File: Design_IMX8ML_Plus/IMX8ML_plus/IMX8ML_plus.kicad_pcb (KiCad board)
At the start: 6 copper layers, 50 x 82 mm, 154 parts, among them J1 DF40C-100DP-0.4V_51_, J2 DF40C-100DP-0.4V_51_, J3 DF40C-100DP-0.4V_51_, U1 MIMX8ML8CVNKZAB, U2 MT53E1536M32D4DT-046 WT:A, U3 SDINBDG4-8G, U4 PCA9450CHNY, U5 MT25QUxxxxxx1xW7, Y1 32.768KHz, Y2 24MHz, Y3 32.768KHz

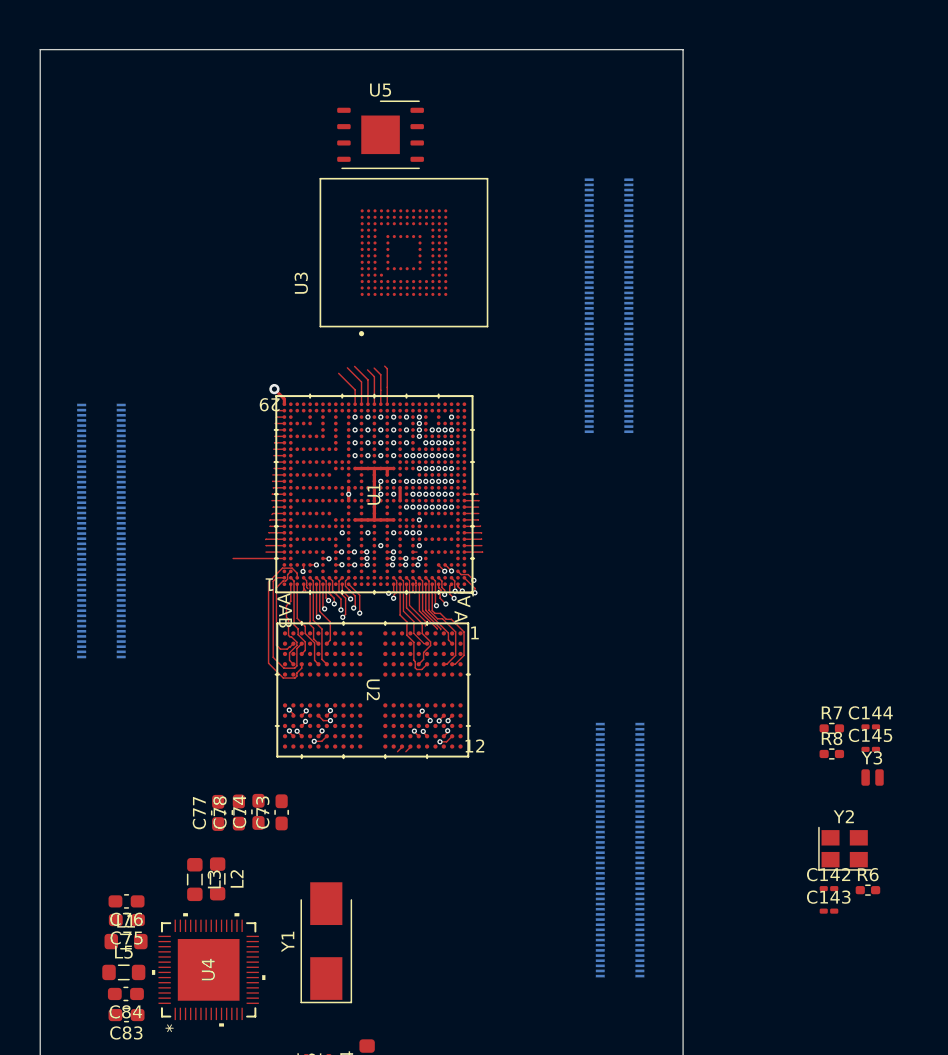
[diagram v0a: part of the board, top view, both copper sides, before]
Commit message: Update schematic and add ethernet interface ksz9131rn
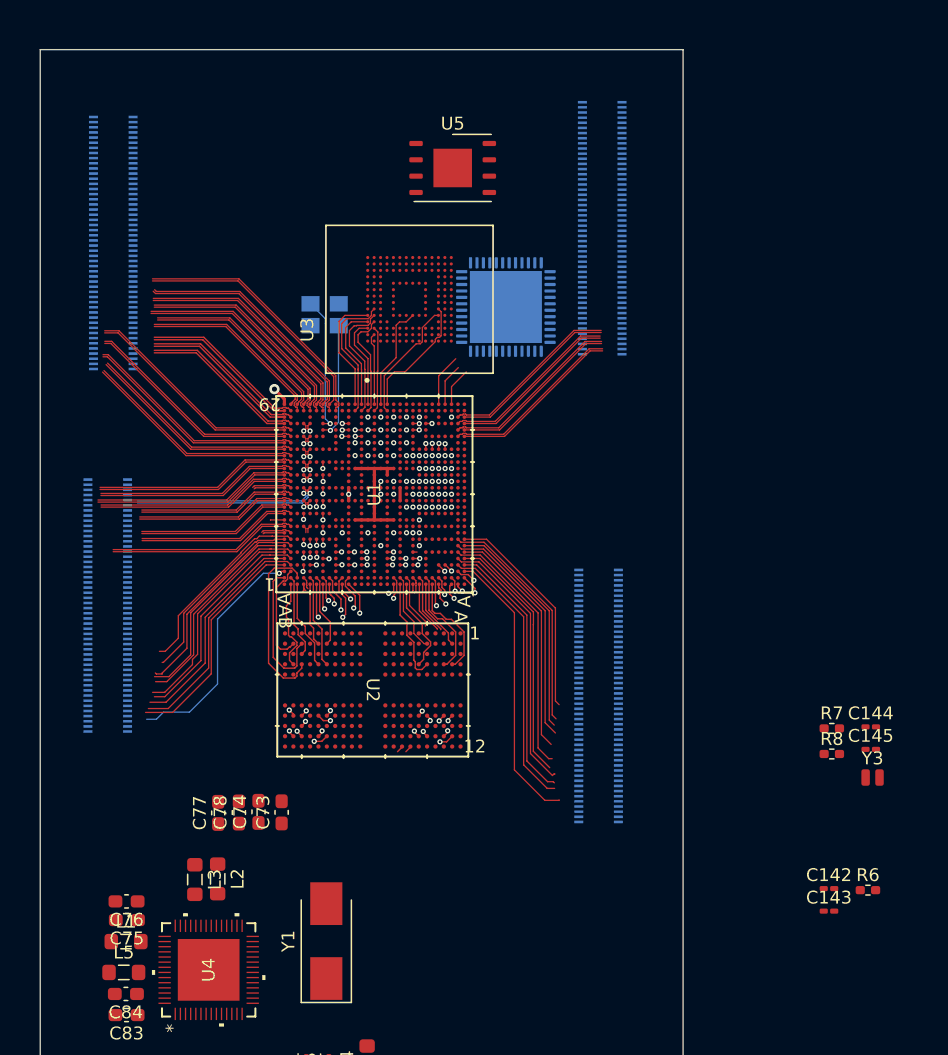
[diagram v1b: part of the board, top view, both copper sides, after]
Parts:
- added J4: DF40C-100DP-0.4V_51_, _W_SBC:HIROSE_DF40C-100DS-0.4V_51_, B.Cu at (153.4, 105.3)
- added U6: KSZ9131RNXI, Package_DFN_QFN:QFN-48-1EP_7x7mm_P0.5mm_EP5.6x5.6mm, B.Cu at (146.2, 75.0)
- Y2: moved to B.Cu
- moved Y2 58.0 mm to (132.1, 75.6), turned to 180 degrees
- moved J1 44.2 mm to (115.2, 98.2)
- moved J2 22.4 mm to (115.7, 70.0), turned to 90 degrees
- moved U5 6.17 mm to (142.1, 64.2)
- moved J3 6.05 mm to (153.7, 68.9), turned to 90 degrees
- moved U3 3.66 mm to (138.7, 74.4)
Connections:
- J1 pad 17: GPIO1_IO00 -> unconnected-(J1-Pad17)
- J1 pad 19: GPIO1_IO01 -> unconnected-(J1-Pad19)
- J1 pad 21: GPIO1_IO02 -> unconnected-(J1-Pad21)
- J1 pad 22: USB1_D_N -> unconnected-(J1-Pad22)
- J1 pad 23: GPIO1_IO03 -> unconnected-(J1-Pad23)
- J1 pad 24: USB1_D_P -> unconnected-(J1-Pad24)
- J1 pad 25: GPIO1_IO04 -> unconnected-(J1-Pad25)
- J1 pad 27: GPIO1_IO05 -> unconnected-(J1-Pad27)
- J1 pad 28: USB1_RX_N -> unconnected-(J1-Pad28)
- J1 pad 29: GPIO1_IO06 -> unconnected-(J1-Pad29)
- J1 pad 30: USB1_RX_P -> unconnected-(J1-Pad30)
- J1 pad 31: GPIO1_IO07 -> unconnected-(J1-Pad31)
- J1 pad 32: USB1_TX_N -> unconnected-(J1-Pad32)
- J1 pad 33: GPIO1_IO08 -> unconnected-(J1-Pad33)
- J1 pad 34: USB1_TX_P -> unconnected-(J1-Pad34)
- J1 pad 35: GPIO1_IO09 -> unconnected-(J1-Pad35)
- J1 pad 37: GPIO1_IO10 -> unconnected-(J1-Pad37)
- J1 pad 38: USB1_BUS -> unconnected-(J1-Pad38)
- J1 pad 39: GPIO1_IO11 -> PCIE_TXN_P
- J1 pad 41: GPIO1_IO12 -> PCIE_TXN_N
- J1 pad 42: PCIE_REF_PAD_CLK_N -> unconnected-(J1-Pad42)
- J1 pad 43: GPIO1_IO13 -> PCIE_RXN_P
- J1 pad 44: PCIE_REF_PAD_CLK_P -> unconnected-(J1-Pad44)
- J1 pad 45: GPIO1_IO14 -> PCIE_RXN_N
- J1 pad 47: GPIO1_IO15 -> unconnected-(J1-Pad47)
- J1 pad 48: PCIE_RXN_N -> unconnected-(J1-Pad48)
- J1 pad 49: unconnected-(J1-Pad49) -> PCIE_REF_PAD_CLK_P
- J1 pad 50: PCIE_RXN_P -> unconnected-(J1-Pad50)
- J1 pad 51: USB2_D_N -> PCIE_REF_PAD_CLK_N
- J1 pad 52: PCIE_TXN_N -> unconnected-(J1-Pad52)
- J1 pad 53: USB2_D_P -> unconnected-(J1-Pad53)
- J1 pad 54: PCIE_TXN_P -> unconnected-(J1-Pad54)
- J1 pad 57: USB2_RX_N -> unconnected-(J1-Pad57)
- J1 pad 58: CSI2_D0_N -> unconnected-(J1-Pad58)
- J1 pad 59: USB2_RX_P -> unconnected-(J1-Pad59)
- J1 pad 60: CSI2_D0_P -> unconnected-(J1-Pad60)
- J1 pad 61: USB2_TX_N -> GPIO1_IO00
- J1 pad 62: CSI2_D1_N -> unconnected-(J1-Pad62)
- J1 pad 63: USB2_TX_P -> GPIO1_IO01
- J1 pad 64: CSI2_D1_P -> unconnected-(J1-Pad64)
- J1 pad 65: unconnected-(J1-Pad65) -> GPIO1_IO02
- J1 pad 66: CSI2_D2_N -> unconnected-(J1-Pad66)
- J1 pad 67: USB2_BUS -> unconnected-(J1-Pad67)
- J1 pad 68: CSI2_D2_P -> unconnected-(J1-Pad68)
- J1 pad 70: CSI2_D3_N -> unconnected-(J1-Pad70)
- J1 pad 71: DSI1_D0_N -> GPIO1_IO05
- J1 pad 72: DSI2_D3_P -> unconnected-(J1-Pad72)
- J1 pad 73: DSI1_D0_P -> GPIO1_IO06
- J1 pad 75: DSI1_D1_N -> GPIO1_IO07
- J1 pad 76: CSI1_D0_N -> unconnected-(J1-Pad76)
- J1 pad 77: DSI1_D1_P -> GPIO1_IO08
- J1 pad 78: CSI1_D0_P -> unconnected-(J1-Pad78)
- J1 pad 79: DSI1_D2_N -> GPIO1_IO09
- J1 pad 80: CSI1_D1_N -> unconnected-(J1-Pad80)
- J1 pad 81: DSI1_D2_P -> GPIO1_IO10
- J1 pad 82: CSI1_D1_P -> unconnected-(J1-Pad82)
- J1 pad 83: DSI1_D3_N -> GPIO1_IO11
- J1 pad 84: CSI1_D2_N -> unconnected-(J1-Pad84)
- J1 pad 85: DSI1_D3_P -> GPIO1_IO12
- J1 pad 86: CSI1_D2_P -> unconnected-(J1-Pad86)
- J1 pad 87: unconnected-(J1-Pad87) -> GPIO1_IO13
- J1 pad 88: CSI1_D3_N -> unconnected-(J1-Pad88)
- J1 pad 89: unconnected-(J1-Pad89) -> GPIO1_IO14
- J1 pad 90: CSI1_D3_P -> unconnected-(J1-Pad90)
- J1 pad 91: unconnected-(J1-Pad91) -> GPIO1_IO15
- J2 pad 10: SAI5_RXD2 -> JTAG_TMS
- J2 pad 100: ENET_TD3 -> unconnected-(J2-Pad100)
- J2 pad 11: SAI1_TXD0 -> HDM_TX2_N
- J2 pad 12: SAI5_RXD3 -> JTAG_TDO
- J2 pad 13: SAI1_TXD1 -> HDM_TX1_P
- J2 pad 14: SAI5_MCLK -> JTAG_TDI
- J2 pad 15: SAI1_TXD2 -> HDM_TX1_N
- J2 pad 16: SAI5_RXC -> JTAG_TCK
- J2 pad 17: SAI1_TXD3 -> HDM_TX0_P
- J2 pad 18: SAI5_RXFS -> JTAG_MOD
- J2 pad 19: SAI1_TXD4 -> HDM_TX0_N
- J2 pad 21: SAI1_TXD5 -> unconnected-(J2-Pad21)
- J2 pad 22: unconnected-(J2-Pad22) -> CLKOUT2
- J2 pad 23: SAI1_TXD6 -> HDM_HPD
- J2 pad 24: SAI2_MCLK -> CLKOUT1
- J2 pad 25: SAI1_RXD7 -> HDM_DDC_SDA
- J2 pad 26: SAI2_RXC -> CLKIN2
- J2 pad 27: unconnected-(J2-Pad27) -> HDM_DDC_SCL
- J2 pad 28: SAI2_RXFS -> CLKIN1
- J2 pad 29: SAI1_MCLK -> HDM_CEC
- J2 pad 30: SAI2_TXC -> unconnected-(J2-Pad30)
- J2 pad 31: SAI1_RXC -> unconnected-(J2-Pad31)
- J2 pad 32: SAI2_TXFS -> BOOT_MODE3
- J2 pad 33: SAI1_RXFS -> unconnected-(J2-Pad33)
- J2 pad 34: unconnected-(J2-Pad34) -> BOOT_MODE2
- J2 pad 35: SAI1_TXC -> unconnected-(J2-Pad35)
- J2 pad 36: SAI2_RXD0 -> BOOT_MODE1
- J2 pad 37: SAi1_TXFS -> LVDS1_CLK_N
- J2 pad 38: SAI2_TXD0 -> BOOT_MODE0
- J2 pad 39: I2C1_SCL -> LVDS1_CLK_P
- J2 pad 41: I2C1_SDA -> LVDS1_D3_P
- J2 pad 42: SAI3_MCLK -> unconnected-(J2-Pad42)
- J2 pad 43: unconnected-(J2-Pad43) -> LVDS1_D3_N
- J2 pad 44: SAI3_RXC -> SDC1_STROBE
- J2 pad 45: I2C3_SDA -> LVDS1_D2_P
- J2 pad 46: SAI3_RXD -> SDC1_RESET_B
- J2 pad 47: I2C3_SCL -> LVDS1_D2_N
- J2 pad 48: SAI3_RXFS -> SDC1_DATA7
- J2 pad 49: unconnected-(J2-Pad49) -> LVDS1_D1_P
- J2 pad 5: SAI1_RXD5 -> HDM_TXC_P
- J2 pad 50: SAI3_TXC -> SDC1_DATA6
- J2 pad 51: I2C2_SCL -> LVDS1_D1_N
- J2 pad 52: SAI3_TXD -> SDC1_DATA5
- J2 pad 53: I2C2_SDA -> LVDS1_D0_P
- J2 pad 54: SAI3_TXFS -> SDC1_DATA4
- J2 pad 55: unconnected-(J2-Pad55) -> LVDS1_D0_N
- J2 pad 56: unconnected-(J2-Pad56) -> SDC1_DATA3
- J2 pad 57: I2C4_SDA -> unconnected-(J2-Pad57)
- J2 pad 58: unconnected-(J2-Pad58) -> SDC1_DATA2
- J2 pad 59: I2C4_SCL -> LVDS0_CLK_P
- J2 pad 6: SAI5_RXD0 -> unconnected-(J2-Pad6)
- J2 pad 60: unconnected-(J2-Pad60) -> SDC1_DATA1
- J2 pad 61: unconnected-(J2-Pad61) -> LVDS0_CLK_N
- J2 pad 62: SAI1_RXD0 -> SDC1_DATA0
- J2 pad 63: UART1_RXD -> LVDS0_D3_P
- J2 pad 64: SAI1_RXD1 -> SDC1_CMD
- J2 pad 65: UART1_TXD -> LVDS0_D3_N
- J2 pad 66: SAI1_RXD2 -> SDC1_CLK
- J2 pad 67: UART2_RXD -> LVDS0_D2_P
- J2 pad 68: SAI1_RXD3 -> unconnected-(J2-Pad68)
- J2 pad 69: UART2_TXD -> LVDS0_D2_N
- J2 pad 7: SAI1_RXD6 -> HDM_TXC_N
- J2 pad 70: SAI1_RXD4 -> SDC2_WP
- J2 pad 71: UART3_RXD -> LVDS0_D1_P
- J2 pad 72: unconnected-(J2-Pad72) -> SDC2_RESET_B
- J2 pad 73: UART3_TXD -> LVDS0_D1_N
- J2 pad 74: ENET_TXC -> SDC2_DATA3
- J2 pad 75: UART4_RXD -> LVDS0_D0_P
- J2 pad 76: ENET_TX_CTL -> SDC2_DATA2
- J2 pad 77: UART4_TXD -> LVDS0_D0_N
- J2 pad 78: ENET_RXC -> SDC2_DATA1
- J2 pad 8: SAI5_RXD1 -> unconnected-(J2-Pad8)
- J2 pad 80: ENET_RX_CTL -> SDC2_DATA0
- J2 pad 82: ENET_MDIO -> SDC2_CMD
- J2 pad 83: CSI1_CLK_P -> unconnected-(J2-Pad83)
- J2 pad 84: ENET_MDC -> SDC2_CLK
- J2 pad 85: CSI1_CLK_N -> unconnected-(J2-Pad85)
- J2 pad 86: ENET_RD0 -> SDC2_CD_B
- J2 pad 88: ENET_RD1 -> unconnected-(J2-Pad88)
- J2 pad 89: CSI2_CLK_P -> unconnected-(J2-Pad89)
- J2 pad 9: SAI1_RXD7 -> HDM_TX2_P
- J2 pad 90: ENET_RD2 -> unconnected-(J2-Pad90)
- J2 pad 91: CSI2_CLK_N -> unconnected-(J2-Pad91)
- J2 pad 92: ENET_RD3 -> unconnected-(J2-Pad92)
- J2 pad 94: ENET_TD0 -> unconnected-(J2-Pad94)
- J2 pad 95: DSI1_CLK_P -> unconnected-(J2-Pad95)
- J2 pad 96: ENET_TD1 -> unconnected-(J2-Pad96)
- J2 pad 97: DSI1_CLK_N -> unconnected-(J2-Pad97)
- J2 pad 98: ENET_TD2 -> unconnected-(J2-Pad98)
- J3 pad 11: LVDS0_D0_N -> unconnected-(J3-Pad11)
- J3 pad 13: LVDS0_D0_P -> unconnected-(J3-Pad13)
- J3 pad 15: LVDS0_D1_N -> unconnected-(J3-Pad15)
- J3 pad 16: SDC2_CD_B -> unconnected-(J3-Pad16)
- J3 pad 17: LVDS0_D1_P -> unconnected-(J3-Pad17)
- J3 pad 18: SDC2_CLK -> unconnected-(J3-Pad18)
- J3 pad 19: LVDS0_D2_N -> unconnected-(J3-Pad19)
- J3 pad 20: SDC2_CMD -> unconnected-(J3-Pad20)
- J3 pad 21: LVDS0_D2_P -> unconnected-(J3-Pad21)
- J3 pad 22: SDC2_DATA0 -> unconnected-(J3-Pad22)
- J3 pad 23: LVDS0_D3_N -> unconnected-(J3-Pad23)
- J3 pad 24: SDC2_DATA1 -> unconnected-(J3-Pad24)
- J3 pad 25: LVDS0_D3_P -> unconnected-(J3-Pad25)
- J3 pad 26: SDC2_DATA2 -> unconnected-(J3-Pad26)
- J3 pad 27: LVDS0_CLK_N -> unconnected-(J3-Pad27)
- J3 pad 28: SDC2_DATA3 -> unconnected-(J3-Pad28)
- J3 pad 29: LVDS0_CLK_P -> SAI1_RXD5
- J3 pad 30: SDC2_RESET_B -> unconnected-(J3-Pad30)
- J3 pad 31: unconnected-(J3-Pad31) -> SAI1_RXD6
- J3 pad 32: SDC2_WP -> SAI5_RXD0
- J3 pad 33: LVDS1_D0_N -> SAI1_RXD7
- J3 pad 34: unconnected-(J3-Pad34) -> SAI5_RXD1
- J3 pad 35: LVDS1_D0_P -> SAI1_TXD0
- J3 pad 36: SDC1_CLK -> SAI5_RXD2
- J3 pad 37: LVDS1_D1_N -> SAI1_TXD1
- J3 pad 38: SDC1_CMD -> SAI5_RXD3
- J3 pad 39: LVDS1_D1_P -> SAI1_TXD2
- J3 pad 40: SDC1_DATA0 -> SAI5_MCLK
- J3 pad 41: LVDS1_D2_N -> SAI1_TXD3
- J3 pad 42: SDC1_DATA1 -> SAI5_RXC
- J3 pad 43: LVDS1_D2_P -> SAI1_TXD4
- J3 pad 44: SDC1_DATA2 -> SAI5_RXFS
- J3 pad 45: LVDS1_D3_N -> SAI1_TXD5
- J3 pad 46: SDC1_DATA3 -> unconnected-(J3-Pad46)
- J3 pad 47: LVDS1_D3_P -> SAI1_TXD6
- J3 pad 48: SDC1_DATA4 -> unconnected-(J3-Pad48)
- J3 pad 49: LVDS1_CLK_P -> SAI1_RXD7
- J3 pad 50: SDC1_DATA5 -> unconnected-(J3-Pad50)
- J3 pad 51: LVDS1_CLK_N -> unconnected-(J3-Pad51)
- J3 pad 52: SDC1_DATA6 -> unconnected-(J3-Pad52)
- J3 pad 54: SDC1_DATA7 -> unconnected-(J3-Pad54)
- J3 pad 56: SDC1_RESET_B -> unconnected-(J3-Pad56)
- J3 pad 58: SDC1_STROBE -> unconnected-(J3-Pad58)
- J3 pad 59: HDM_CEC -> unconnected-(J3-Pad59)
- J3 pad 61: HDM_DDC_SCL -> unconnected-(J3-Pad61)
- J3 pad 63: HDM_DDC_SDA -> unconnected-(J3-Pad63)
- J3 pad 64: BOOT_MODE0 -> unconnected-(J3-Pad64)
- J3 pad 65: HDM_HPD -> unconnected-(J3-Pad65)
- J3 pad 66: BOOT_MODE1 -> TXRXA_N
- J3 pad 68: BOOT_MODE2 -> TXRXA_P
- J3 pad 69: HDM_TX0_N -> unconnected-(J3-Pad69)
- J3 pad 70: BOOT_MODE3 -> unconnected-(J3-Pad70)
- J3 pad 71: HDM_TX0_P -> unconnected-(J3-Pad71)
- J3 pad 72: unconnected-(J3-Pad72) -> TXRXB_N
- J3 pad 73: HDM_TX1_N -> unconnected-(J3-Pad73)
- J3 pad 74: CLKIN1 -> TXRXB_P
- J3 pad 75: HDM_TX1_P -> unconnected-(J3-Pad75)
- J3 pad 76: CLKIN2 -> unconnected-(J3-Pad76)
- J3 pad 77: HDM_TX2_N -> unconnected-(J3-Pad77)
- J3 pad 78: CLKOUT1 -> TXRXC_P
- J3 pad 79: HDM_TX2_P -> unconnected-(J3-Pad79)
- J3 pad 80: CLKOUT2 -> TXRXC_N
- J3 pad 81: HDM_TXC_N -> unconnected-(J3-Pad81)
- J3 pad 83: HDM_TXC_P -> unconnected-(J3-Pad83)
- J3 pad 84: JTAG_MOD -> TXRXD_N
- J3 pad 86: JTAG_TCK -> TXRXD_P
- J3 pad 88: JTAG_TDI -> unconnected-(J3-Pad88)
- J3 pad 90: JTAG_TDO -> unconnected-(J3-Pad90)
- J3 pad 92: JTAG_TMS -> unconnected-(J3-Pad92)
- U1 pad A11: USB1_BUS -> USB1_VBUS
- U1 pad A21: DSI2_D3_P -> CSI2_D3_P
- U1 pad AC22: HDM_DDC_SCL -> HDMI_DDC_SCL
- U1 pad AD22: HDM_CEC -> HDMI_CEC
- U1 pad AE22: HDM_HPD -> HDMI_HPD
- U1 pad AF22: HDM_DDC_SDA -> HDMI_DDC_SDA
- U1 pad AH24: HDM_TXC_P -> HDMI_TXC_P
- U1 pad AH25: HDM_TX0_P -> HDMI_TX0_P
- U1 pad AH26: HDM_TX1_P -> HDMI_TX1_P
- U1 pad AH27: HDM_TX2_P -> HDMI_TX2_P
- U1 pad AJ24: HDM_TXC_N -> HDMI_TXC_N
- U1 pad AJ25: HDM_TX0_N -> HDMI_TX0_N
- U1 pad AJ26: HDM_TX1_N -> HDMI_TX1_N
- U1 pad AJ27: HDM_TX2_N -> HDMI_TX2_N
- U1 pad D12: USB2_BUS -> USB2_VBUS
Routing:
- net /Processor/storage/QSPIA_DATA3: track 0.00 -> 33.5 mm, vias 0 -> 1
- net /Processor/storage/QSPIA_SCLK: track 0.00 -> 30.4 mm, vias 0 -> 1
- net /Processor/storage/QSPIA_DATA0: track 0.00 -> 29.7 mm, vias 0 -> 1
- net /Processor/storage/QSPIA_nSS0: track 0.00 -> 26.0 mm, vias 0 -> 1
- net /Processor/storage/QSPIA_DATA1: track 0.00 -> 25.3 mm, vias 0 -> 1
- net /Processor/storage/QSPIA_DATA2: track 0.00 -> 24.4 mm, vias 0 -> 1
- net CSI1_D0_N: track 0.00 -> 23.7 mm, vias 0 -> 1
- net CSI1_D0_P: track 0.00 -> 23.3 mm, vias 0 -> 1
- net CSI1_D1_N: track 0.00 -> 22.7 mm, vias 0 -> 1
- net CSI1_D1_P: track 0.00 -> 22.3 mm, vias 0 -> 1
- net UART1_TXD: track 0.00 -> 21.9 mm
- net UART2_TXD: track 0.00 -> 21.5 mm
- net GPIO1_IO07: track 0.00 -> 21.2 mm, vias 0 -> 1
- net CSI1_CLK_N: track 0.00 -> 21.0 mm, vias 0 -> 1
- net UART4_TXD: track 0.00 -> 21.0 mm
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
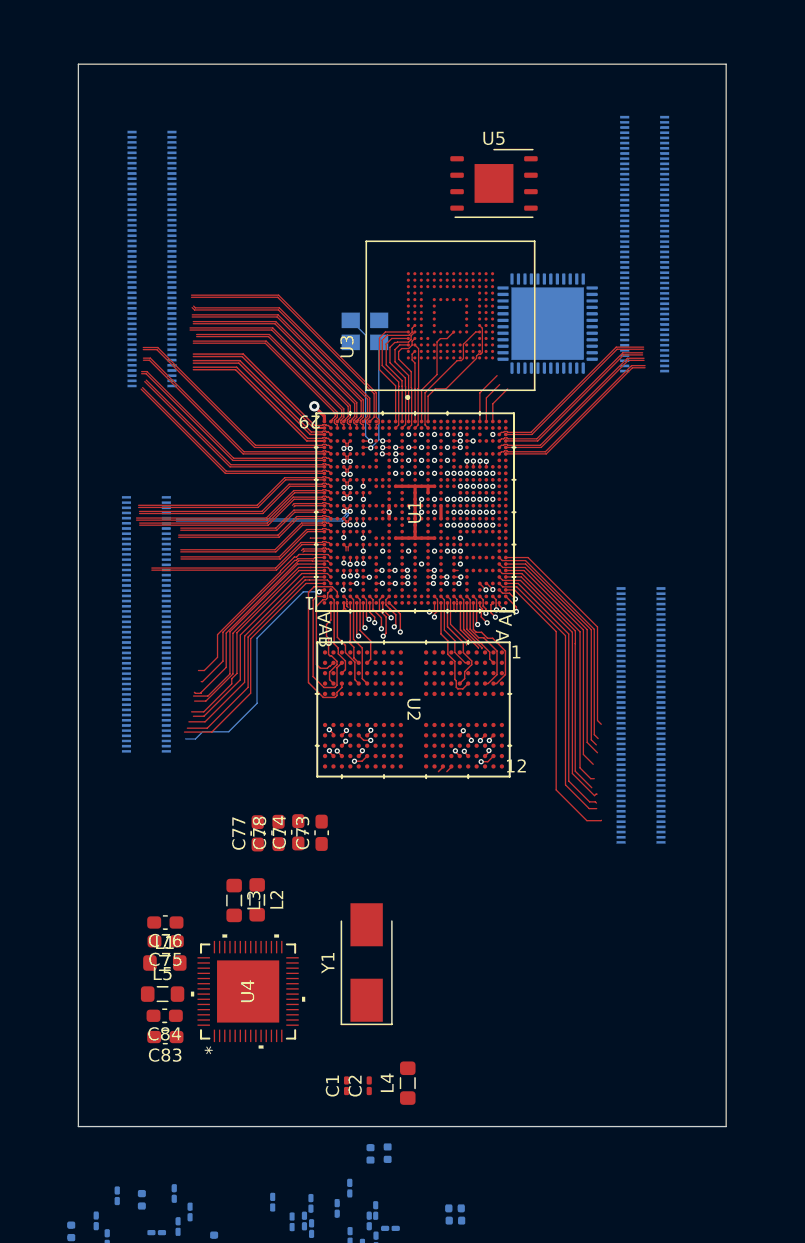
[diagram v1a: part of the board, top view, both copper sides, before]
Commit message: Add power layer
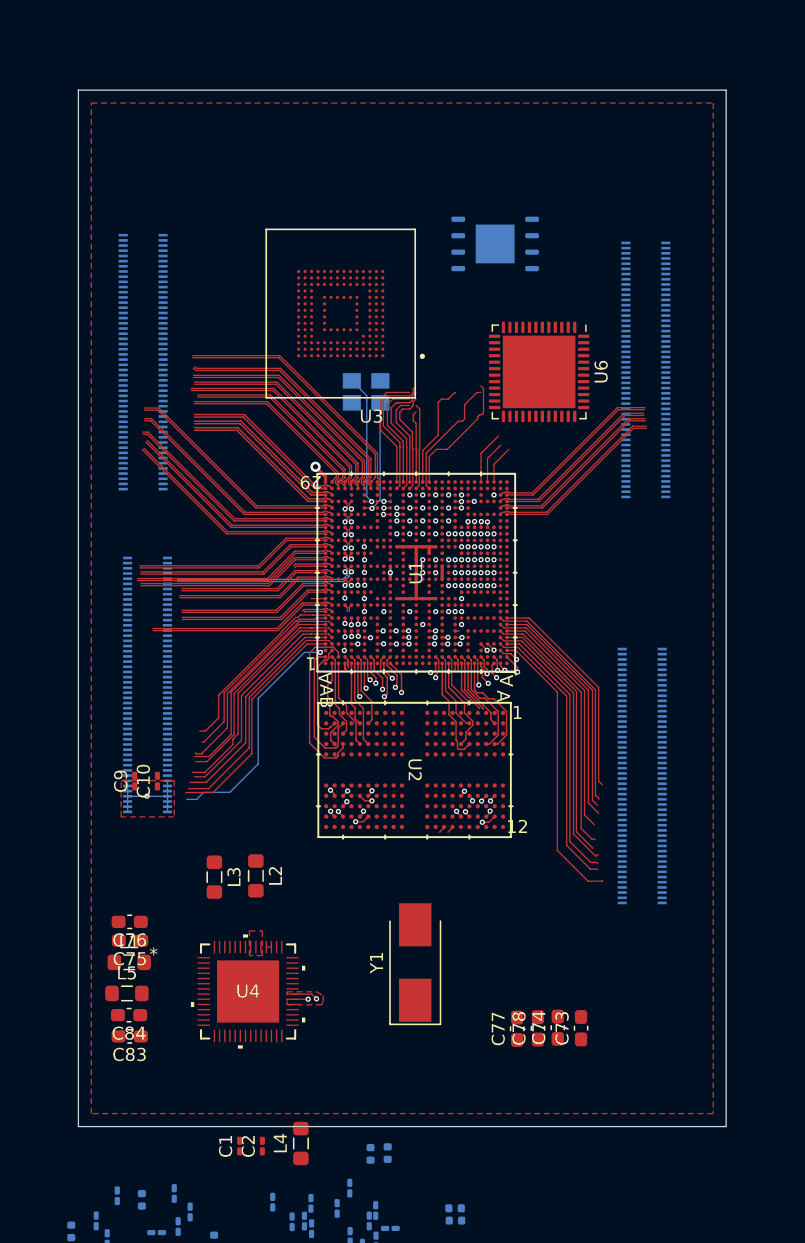
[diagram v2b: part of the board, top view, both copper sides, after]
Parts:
- added C10: 10uF, Capacitor_SMD:C_0201_0603Metric_Pad0.64x0.40mm_HandSolder, F.Cu at (116.1, 110.3)
- added C9: 10uF, Capacitor_SMD:C_0201_0603Metric_Pad0.64x0.40mm_HandSolder, F.Cu at (114.3, 110.3)
- U5: moved to B.Cu
- U6: moved to F.Cu
- moved C74 25.1 mm to (147.0, 129.4)
- moved C73 25.1 mm to (148.8, 129.4)
- moved C77 25.1 mm to (143.9, 129.4)
- moved C78 25.1 mm to (145.5, 129.4)
- moved J3 9.71 mm to (153.8, 78.6)
- moved L4 9.47 mm to (127.2, 138.3)
- moved C1 9.47 mm to (122.5, 138.5)
- moved C2 9.47 mm to (124.2, 138.5)
- moved U3 8.47 mm to (130.2, 74.2), turned to 180 degrees
- moved J2 7.99 mm to (115.0, 78.0)
- moved J1 4.67 mm to (115.3, 102.9)
- moved J4 4.67 mm to (153.5, 109.9)
- moved U1 4.67 mm to (136.1, 94.2)
- moved Y2 4.67 mm to (132.2, 80.3)
- moved U5 4.67 mm to (142.2, 68.9), turned to 180 degrees
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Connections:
- J1 pad 100: unconnected-(J1-Pad100) -> VDD_SYS
- J1 pad 11: unconnected-(J1-Pad11) -> PCIE_TXN_P
- J1 pad 13: unconnected-(J1-Pad13) -> PCIE_TXN_N
- J1 pad 15: unconnected-(J1-Pad15) -> PCIE_RXN_P
- J1 pad 17: unconnected-(J1-Pad17) -> PCIE_RXN_N
- J1 pad 21: unconnected-(J1-Pad21) -> PCIE_REF_PAD_CLK_P
- J1 pad 23: unconnected-(J1-Pad23) -> PCIE_REF_PAD_CLK_N
- J1 pad 33: unconnected-(J1-Pad33) -> GPIO1_IO00
- J1 pad 35: unconnected-(J1-Pad35) -> GPIO1_IO01
- J1 pad 37: unconnected-(J1-Pad37) -> GPIO1_IO02
- J1 pad 39: PCIE_TXN_P -> unconnected-(J1-Pad39)
- J1 pad 41: PCIE_TXN_N -> unconnected-(J1-Pad41)
- J1 pad 43: PCIE_RXN_P -> GPIO1_IO05
- J1 pad 45: PCIE_RXN_N -> GPIO1_IO06
- J1 pad 47: unconnected-(J1-Pad47) -> GPIO1_IO07
- J1 pad 49: PCIE_REF_PAD_CLK_P -> GPIO1_IO08
- J1 pad 51: PCIE_REF_PAD_CLK_N -> GPIO1_IO09
- J1 pad 53: unconnected-(J1-Pad53) -> GPIO1_IO10
- J1 pad 55: unconnected-(J1-Pad55) -> GPIO1_IO11
- J1 pad 57: unconnected-(J1-Pad57) -> GPIO1_IO12
- J1 pad 59: unconnected-(J1-Pad59) -> GPIO1_IO13
- J1 pad 61: GPIO1_IO00 -> GPIO1_IO14
- J1 pad 63: GPIO1_IO01 -> GPIO1_IO15
- J1 pad 65: GPIO1_IO02 -> unconnected-(J1-Pad65)
- J1 pad 71: GPIO1_IO05 -> unconnected-(J1-Pad71)
- J1 pad 73: GPIO1_IO06 -> unconnected-(J1-Pad73)
- J1 pad 75: GPIO1_IO07 -> GND
- J1 pad 76: unconnected-(J1-Pad76) -> GND
- J1 pad 77: GPIO1_IO08 -> GND
- J1 pad 78: unconnected-(J1-Pad78) -> GND
- J1 pad 79: GPIO1_IO09 -> GND
- J1 pad 80: unconnected-(J1-Pad80) -> GND
- J1 pad 81: GPIO1_IO10 -> GND
- J1 pad 82: unconnected-(J1-Pad82) -> GND
- J1 pad 83: GPIO1_IO11 -> GND
- J1 pad 84: unconnected-(J1-Pad84) -> GND
- J1 pad 85: GPIO1_IO12 -> GND
- J1 pad 86: unconnected-(J1-Pad86) -> GND
- J1 pad 87: GPIO1_IO13 -> GND
- J1 pad 88: unconnected-(J1-Pad88) -> GND
- J1 pad 89: GPIO1_IO14 -> VDD_SYS
- J1 pad 90: unconnected-(J1-Pad90) -> VDD_SYS
- J1 pad 91: GPIO1_IO15 -> VDD_SYS
- J1 pad 92: unconnected-(J1-Pad92) -> VDD_SYS
- J1 pad 93: unconnected-(J1-Pad93) -> VDD_SYS
- J1 pad 94: unconnected-(J1-Pad94) -> VDD_SYS
- J1 pad 95: unconnected-(J1-Pad95) -> VDD_SYS
- J1 pad 96: unconnected-(J1-Pad96) -> VDD_SYS
- J1 pad 97: unconnected-(J1-Pad97) -> VDD_SYS
- J1 pad 98: unconnected-(J1-Pad98) -> VDD_SYS
- J1 pad 99: unconnected-(J1-Pad99) -> VDD_SYS
- J3 pad 60: unconnected-(J3-Pad60) -> LED1
- J3 pad 62: unconnected-(J3-Pad62) -> LED2
- U6 pad 10: TXRXC_P -> TXRXD_P
- U6 pad 15: unconnected-(U6A-LED2/PHYAD1-Pad15) -> LED2
- U6 pad 16: unconnected-(U6B-DVDDH-Pad16) -> Net-(U6B-DVDDH-Pad16)
- U6 pad 17: unconnected-(U6A-LED1/PME_N1//PHYAD0-Pad17) -> LED1
- U6 pad 18: unconnected-(U6B-DVDDL-Pad18) -> Net-(U6B-DVDDL-Pad18)
- U6 pad 23: unconnected-(U6B-DVDDL-Pad23) -> Net-(U6B-DVDDL-Pad18)
- U6 pad 26: unconnected-(U6B-DVDDL-Pad26) -> Net-(U6B-DVDDL-Pad18)
- U6 pad 29: unconnected-(U6B-VSS-Pad29) -> GND
- U6 pad 30: unconnected-(U6B-DVDDL-Pad30) -> Net-(U6B-DVDDL-Pad18)
- U6 pad 34: unconnected-(U6B-DVDDH-Pad34) -> Net-(U6B-DVDDH-Pad16)
- U6 pad 39: unconnected-(U6B-DVDDL-Pad39) -> Net-(U6B-DVDDL-Pad18)
- U6 pad 40: unconnected-(U6B-DVDDH-Pad40) -> Net-(U6B-DVDDH-Pad16)
- U6 pad 49: unconnected-(U6B-P_VSS-Pad49) -> GND
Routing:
- net VDD_SYS: track 0.00 -> 11.1 mm, vias 0 -> 3
- added copper zone on F.Cu, net GND
- added copper zone on F.Cu, net VDD_SYS
- added copper zone on In2.Cu, net VDD_SYS
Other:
- board size 50 x 82 mm -> 50 x 80 mm
